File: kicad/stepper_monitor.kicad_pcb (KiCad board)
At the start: 2 copper layers, 38.5 x 43 mm, 52 parts, among them J1 Conn_01x04_Male, J2 Conn_01x04_Male, J3 Conn_01x02_Male, J4 USB_C_Receptacle_USB2.0, J5 JTAG, Q1 UMH3N, Q2 PJA3439, SW1 SW_Push, U1 CP2102N-A01-GQFN28, U2 AMS1117-3.3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

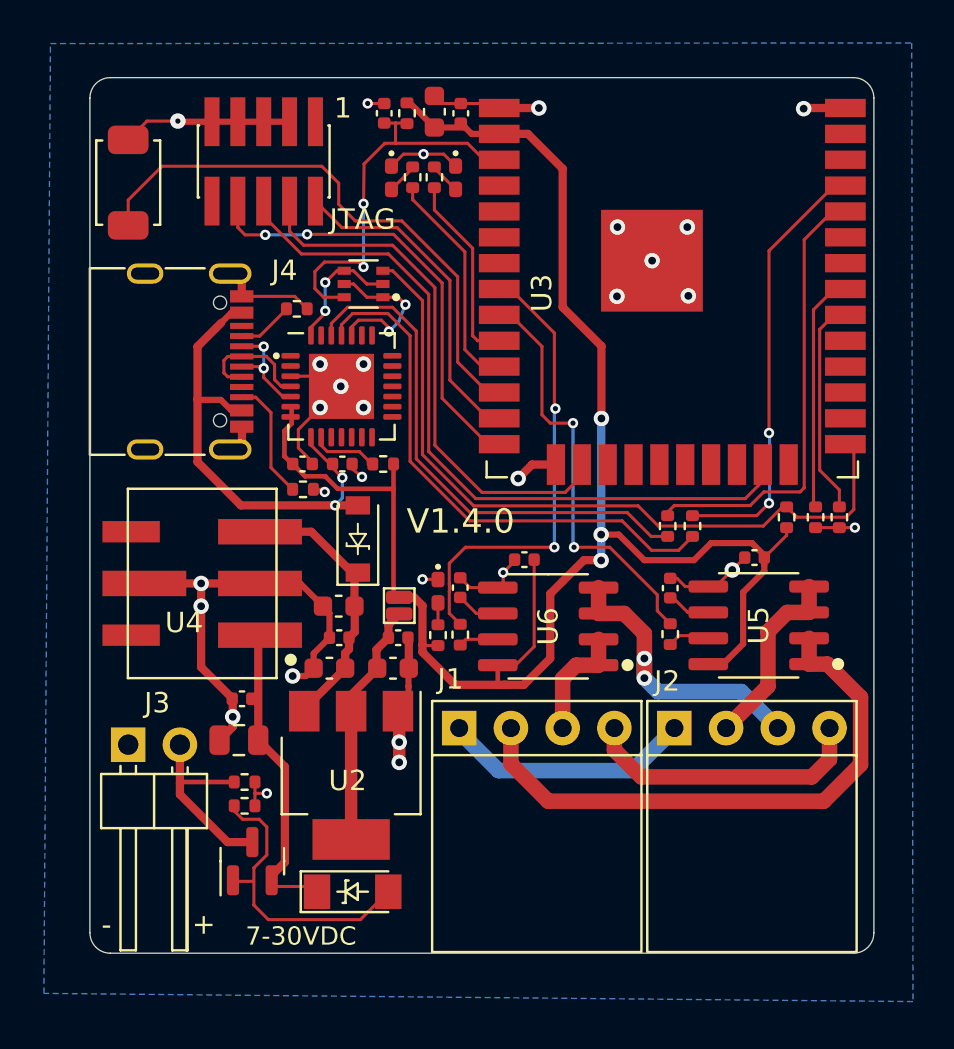
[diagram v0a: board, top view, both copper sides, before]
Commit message: Updated analog input pins.
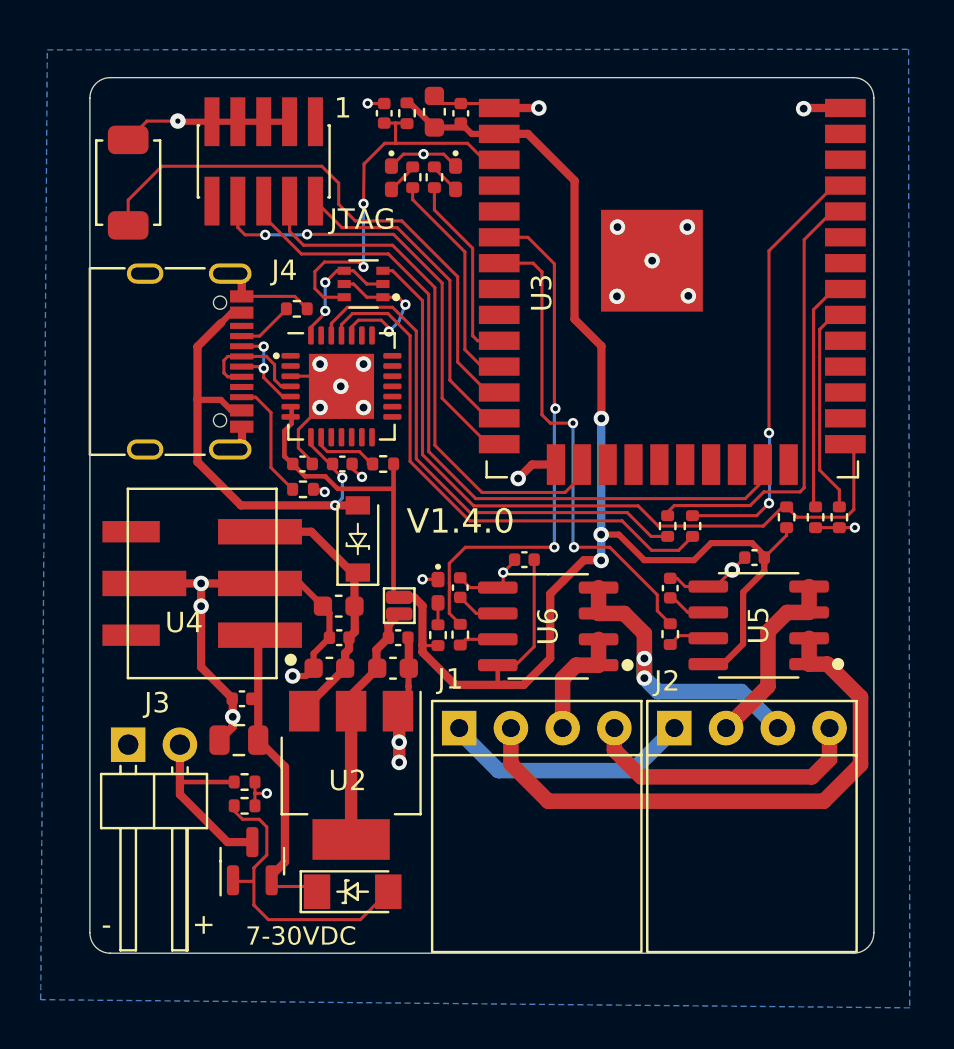
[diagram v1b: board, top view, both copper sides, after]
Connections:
- U3 pad 6: unconnected-(U3-Pad6) -> CHA
- U3 pad 7: unconnected-(U3-Pad7) -> CHB
- U3 pad 8: CHA -> unconnected-(U3-Pad8)
- U3 pad 9: CHB -> unconnected-(U3-Pad9)
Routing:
- net CHB: track 20.6 -> 23.8 mm
- net CHA: track 22.9 -> 25.9 mm
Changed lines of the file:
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@@
   (net 49 "Net-(J1-Pad1)")
   (net 50 "Net-(J1-Pad2)")
-  (net 51 "unconnected-(U3-Pad7)")
-  (net 52 "unconnected-(U3-Pad6)")
+  (net 51 "unconnected-(U3-Pad8)")
+  (net 52 "unconnected-(U3-Pad9)")
   (net 53 "unconnected-(U3-Pad5)")
   (net 54 "unconnected-(U3-Pad4)")
@@
       (net 53 "unconnected-(U3-Pad5)") (pinfunction "SENSOR_VN") (pintype "input+no_connect"))
     (pad "6" smd rect (at -2.655 8.5 270) (size 0.9 2) (layers "F.Cu" "F.Paste" "F.Mask")
-      (net 52 "unconnected-(U3-Pad6)") (pinfunction "IO34") (pintype "input+no_connect"))
+      (net 79 "CHA") (pinfunction "IO34") (pintype "input"))
     (pad "7" smd rect (at -1.385 8.5 270) (size 0.9 2) (layers "F.Cu" "F.Paste" "F.Mask")
-      (net 51 "unconnected-(U3-Pad7)") (pinfunction "IO35") (pintype "input+no_connect"))
+      (net 78 "CHB") (pinfunction "IO35") (pintype "input"))
     (pad "8" smd rect (at -0.115 8.5 270) (size 0.9 2) (layers "F.Cu" "F.Paste" "F.Mask")
-      (net 79 "CHA") (pinfunction "IO32") (pintype "bidirectional"))
+      (net 51 "unconnected-(U3-Pad8)") (pinfunction "IO32") (pintype "bidirectional+no_connect"))
     (pad "9" smd rect (at 1.155 8.5 270) (size 0.9 2) (layers "F.Cu" "F.Paste" "F.Mask")
-      (net 78 "CHB") (pinfunction "IO33") (pintype "bidirectional"))
+      (net 52 "unconnected-(U3-Pad9)") (pinfunction "IO33") (pintype "bidirectional+no_connect"))
     (pad "10" smd rect (at 2.425 8.5 270) (size 0.9 2) (layers "F.Cu" "F.Paste" "F.Mask")
       (net 75 "LED2") (pinfunction "IO25") (pintype "bidirectional"))
@@
   (segment (start 13.6632 -24.206) (end 13.6632 -24.0008) (width 0.1524) (layer "F.Cu") (net 18))
   (segment (start 11.3538 -25.388284) (end 11.3538 -24.9406) (width 0.1524) (layer "F.Cu") (net 18))
-  (segment (start 23.2154 -38.5294) (end 23.2154 -31.7226) (width 0.4064) (layer "F.Cu") (net 19))
   (segment (start 19.9642 -13.1806) (end 17.9344 -13.1806) (width 0.4064) (layer "F.Cu") (net 19))
   (segment (start 12.1666 -22.807) (end 11.5518 -23.4218) (width 0.2286) (layer "F.Cu") (net 19))
   (segment (start 9.9038 -26.338284) (end 9.9038 -26.0052) (width 0.2286) (layer "F.Cu") (net 19))
   (segment (start 31.0874 -14.1964) (end 32.0802 -15.1892) (width 0.3048) (layer "F.Cu") (net 19))
-  (segment (start 23.2154 -31.7226) (end 25.1204 -29.8176) (width 0.4064) (layer "F.Cu") (net 19))
   (segment (start 15.7056 -41.7616) (end 15.5702 -41.7616) (width 0.3048) (layer "F.Cu") (net 19))
   (segment (start 33.119 -19.5352) (end 33.119 -19.4288) (width 0.3048) (layer "F.Cu") (net 19))
+  (segment (start 20.1004 -40.238) (end 21.5068 -40.238) (width 0.4064) (layer "F.Cu") (net 19))
   (segment (start 34.2138 -20.5236) (end 34.2138 -20.9) (width 0.1524) (layer "F.Cu") (net 19))
+  (segment (start 23.7998 -37.945) (end 23.7998 -31.1382) (width 0.4064) (layer "F.Cu") (net 19))
   (segment (start 20.2944 -13.1806) (end 21.3104 -13.1806) (width 0.4064) (layer "F.Cu") (net 19))
   (segment (start 20.1004 -40.238) (end 18.7412 -40.238) (width 0.3048) (layer "F.Cu") (net 19))
@@
   (segment (start 20.0294 -13.2458) (end 19.9642 -13.1806) (width 0.1524) (layer "F.Cu") (net 19))
   (segment (start 25.0924 -19.302) (end 25.1066 -19.2878) (width 0.3048) (layer "F.Cu") (net 19))
+  (segment (start 23.7998 -31.1382) (end 25.1204 -29.8176) (width 0.4064) (layer "F.Cu") (net 19))
   (segment (start 23.2154 -18.2606) (end 24.2568 -19.302) (width 0.4064) (layer "F.Cu") (net 19))
   (segment (start 17.0942 -15.1088) (end 16.3596 -15.1088) (width 0.1524) (layer "F.Cu") (net 19))
@@
   (segment (start 9.5504 -25.6518) (end 9.5504 -24.4072) (width 0.2286) (layer "F.Cu") (net 19))
   (segment (start 20.0294 -14.1456) (end 20.0294 -13.2458) (width 0.2286) (layer "F.Cu") (net 19))
+  (segment (start 21.5068 -40.238) (end 23.7998 -37.945) (width 0.4064) (layer "F.Cu") (net 19))
   (segment (start 9.9038 -26.0052) (end 9.5504 -25.6518) (width 0.2286) (layer "F.Cu") (net 19))
   (segment (start 32.514 -20.1402) (end 33.119 -19.5352) (width 0.3048) (layer "F.Cu") (net 19))
-  (segment (start 20.1004 -40.238) (end 21.5068 -40.238) (width 0.4064) (layer "F.Cu") (net 19))
-  (segment (start 21.5068 -40.238) (end 23.2154 -38.5294) (width 0.4064) (layer "F.Cu") (net 19))
   (segment (start 27.2286 -19.302) (end 29.667 -19.302) (width 0.3048) (layer "F.Cu") (net 19))
   (segment (start 10.5638 -23.4218) (end 9.9594 -24.0262) (width 0.2286) (layer "F.Cu") (net 19))
@@
   (segment (start 28.702 -21.9942) (end 28.3718 -21.664) (width 0.1524) (layer "F.Cu") (net 77))
   (segment (start 32.4284 -21.9868) (end 28.7094 -21.9868) (width 0.1524) (layer "F.Cu") (net 77))
-  (segment (start 20.1004 -31.348) (end 20.6504 -31.348) (width 0.1524) (layer "F.Cu") (net 78))
-  (segment (start 22.1996 -29.7988) (end 22.1996 -26.4414) (width 0.1524) (layer "F.Cu") (net 78))
+  (segment (start 22.6082 -26.0328) (end 23.7236 -26.0328) (width 0.1524) (layer "F.Cu") (net 78))
+  (segment (start 21.7634 -33.888) (end 22.1996 -33.4518) (width 0.1524) (layer "F.Cu") (net 78))
   (segment (start 23.7744 -19.9368) (end 25.527 -19.9368) (width 0.1524) (layer "F.Cu") (net 78))
+  (segment (start 25.527 -19.9368) (end 27.8638 -17.6) (width 0.1524) (layer "F.Cu") (net 78))
+  (segment (start 27.8638 -16.8146) (end 28.4988 -16.1796) (width 0.1524) (layer "F.Cu") (net 78))
   (segment (start 22.1996 -26.4414) (end 22.6082 -26.0328) (width 0.1524) (layer "F.Cu") (net 78))
-  (segment (start 25.527 -19.9368) (end 27.8638 -17.6) (width 0.1524) (layer "F.Cu") (net 78))
-  (segment (start 22.6082 -26.0328) (end 23.7236 -26.0328) (width 0.1524) (layer "F.Cu") (net 78))
-  (segment (start 27.8638 -16.8146) (end 28.4988 -16.1796) (width 0.1524) (layer "F.Cu") (net 78))
-  (segment (start 20.6504 -31.348) (end 22.1996 -29.7988) (width 0.1524) (layer "F.Cu") (net 78))
+  (segment (start 20.1004 -33.888) (end 21.7634 -33.888) (width 0.1524) (layer "F.Cu") (net 78))
   (segment (start 27.8638 -17.6) (end 27.8638 -16.8146) (width 0.1524) (layer "F.Cu") (net 78))
+  (segment (start 22.1996 -33.4518) (end 22.1996 -26.4414) (width 0.1524) (layer "F.Cu") (net 78))
   (via (at 23.7744 -19.9368) (size 0.508) (drill 0.254) (layers "F.Cu" "B.Cu") (net 78))
   (via (at 23.7236 -26.0328) (size 0.508) (drill 0.254) (layers "F.Cu" "B.Cu") (net 78))
@@
   (segment (start 17.6478 -19.1442) (end 17.6478 -18.142921) (width 0.1524) (layer "F.Cu") (net 79))
   (segment (start 22.8092 -19.9368) (end 18.4404 -19.9368) (width 0.1524) (layer "F.Cu") (net 79))
-  (segment (start 22.8092 -26.7948) (end 22.8092 -30.4592) (width 0.1524) (layer "F.Cu") (net 79))
+  (segment (start 21.5094 -35.158) (end 20.1004 -35.158) (width 0.1524) (layer "F.Cu") (net 79))
+  (segment (start 22.86 -26.744) (end 22.8092 -26.7948) (width 0.1524) (layer "F.Cu") (net 79))
   (segment (start 17.6478 -16.6928) (end 18.1864 -16.1542) (width 0.1524) (layer "F.Cu") (net 79))
   (segment (start 18.4404 -19.9368) (end 17.6478 -19.1442) (width 0.1524) (layer "F.Cu") (net 79))
   (segment (start 17.6478 -17.768279) (end 17.6478 -16.6928) (width 0.1524) (layer "F.Cu") (net 79))
-  (segment (start 20.6504 -32.618) (end 20.1004 -32.618) (width 0.1524) (layer "F.Cu") (net 79))
+  (segment (start 22.8092 -26.7948) (end 22.8092 -33.8582) (width 0.1524) (layer "F.Cu") (net 79))
   (segment (start 17.653 -17.773479) (end 17.6478 -17.768279) (width 0.1524) (layer "F.Cu") (net 79))
-  (segment (start 22.8092 -30.4592) (end 20.6504 -32.618) (width 0.1524) (layer "F.Cu") (net 79))
-  (segment (start 22.86 -26.744) (end 22.8092 -26.7948) (width 0.1524) (layer "F.Cu") (net 79))
+  (segment (start 22.8092 -33.8582) (end 21.5094 -35.158) (width 0.1524) (layer "F.Cu") (net 79))
   (segment (start 17.653 -18.137721) (end 17.653 -17.773479) (width 0.1524) (layer "F.Cu") (net 79))
   (via (at 22.8092 -19.9368) (size 0.508) (drill 0.254) (layers "F.Cu" "B.Cu") (net 79))
@@
     (polygon
       (pts
-        (xy 40.418531 2.375603)
-        (xy -2.261772 1.973719)
-        (xy -1.938703 -44.671884)
-        (xy 40.3606 -44.7018)
+        (xy 40.26332 2.684177)
+        (xy -2.416983 2.282293)
+        (xy -2.093914 -44.36331)
+        (xy 40.205389 -44.393226)
       )
     )

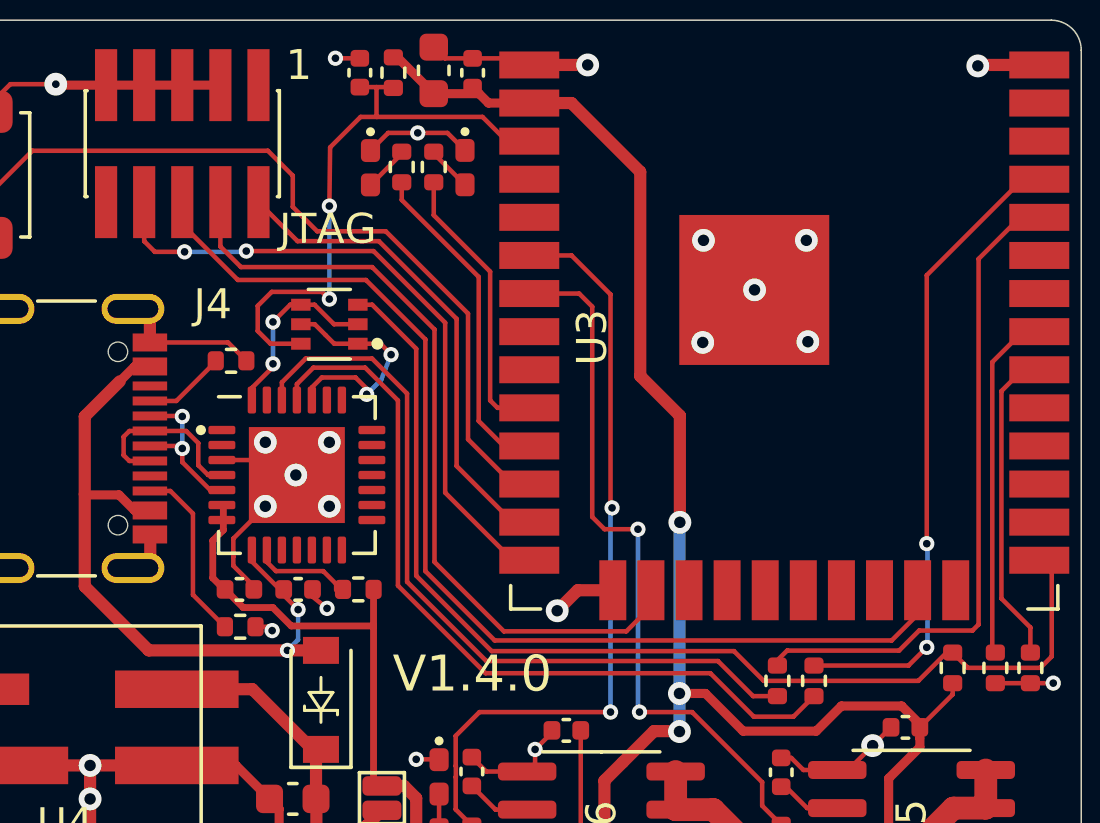
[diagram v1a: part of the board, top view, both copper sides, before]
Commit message: Added test point.
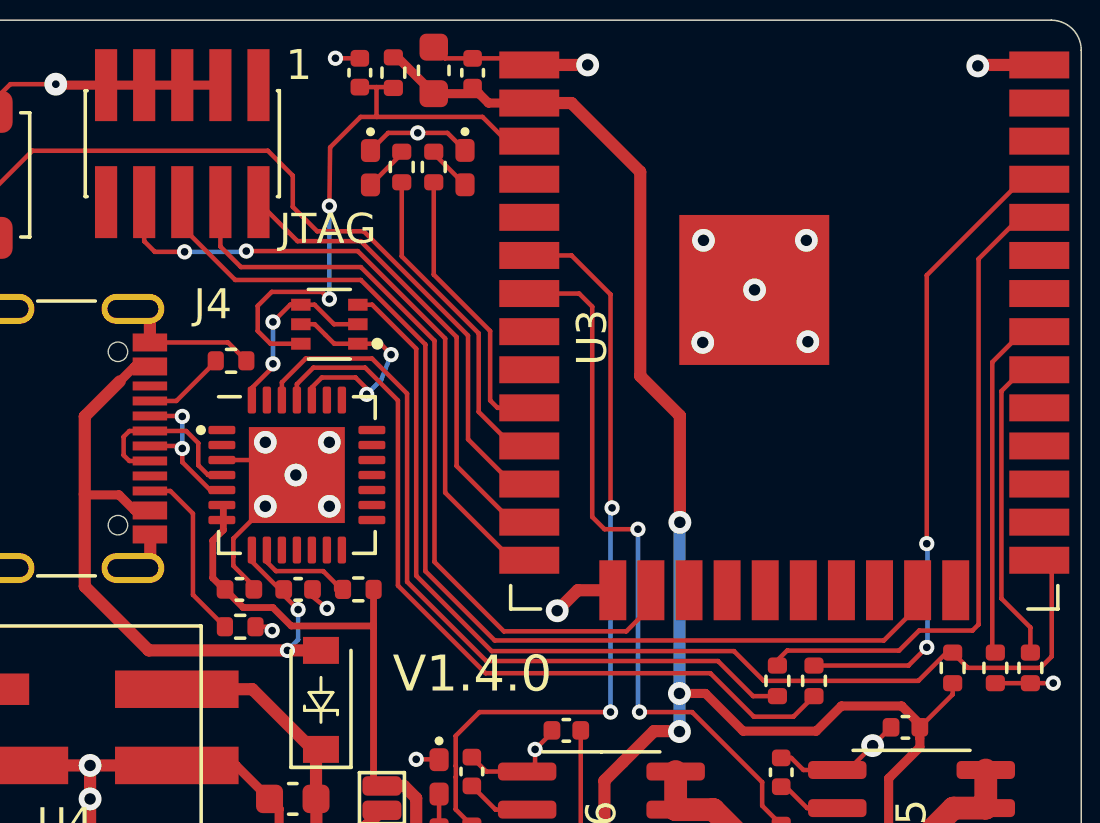
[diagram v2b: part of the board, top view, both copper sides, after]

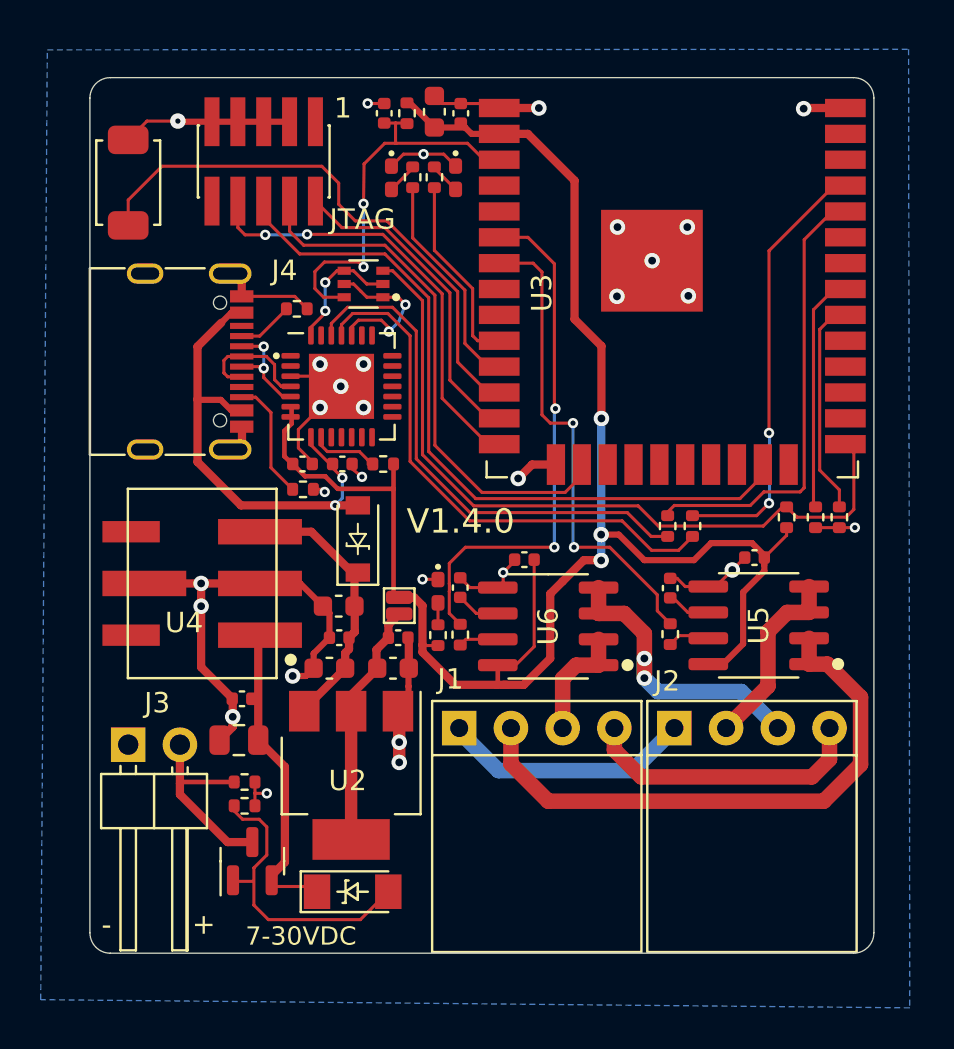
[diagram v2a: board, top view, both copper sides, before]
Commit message: Added ADC capacitors.
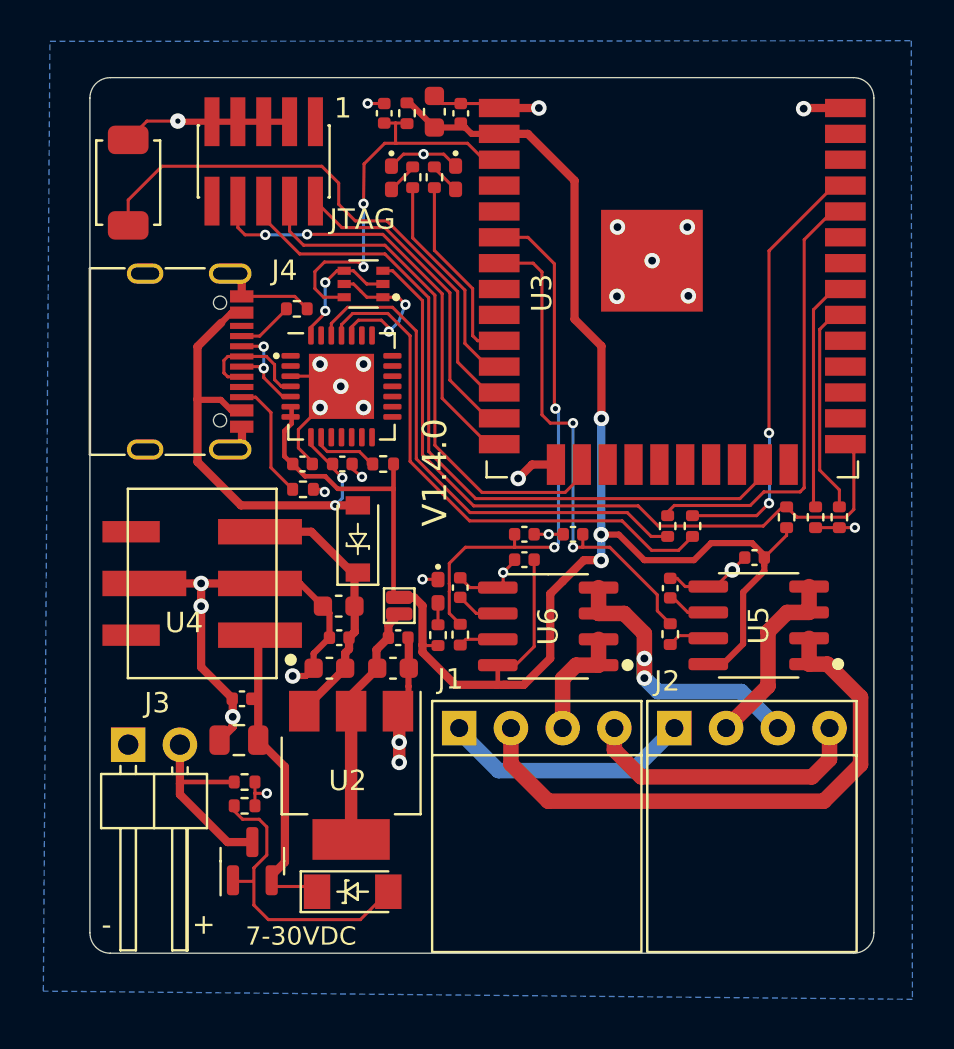
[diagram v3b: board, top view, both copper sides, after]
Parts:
- added C17: 4n7, Capacitor_SMD:C_0402_1005Metric, F.Cu at (23.7, -20.6)
- added C18: 4n7, Capacitor_SMD:C_0402_1005Metric, F.Cu at (21.3, -20.6)
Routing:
- net GNDD: track 77.0 -> 78.4 mm, vias 29 -> 30
- net CHA: track 25.9 -> 26.7 mm
- net CHB: track 23.8 -> 24.5 mm
